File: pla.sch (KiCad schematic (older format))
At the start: 8 parts, among them U12 74LS02, U14 74LS139, U15 74LS175, U16 MOS_251641_PLA

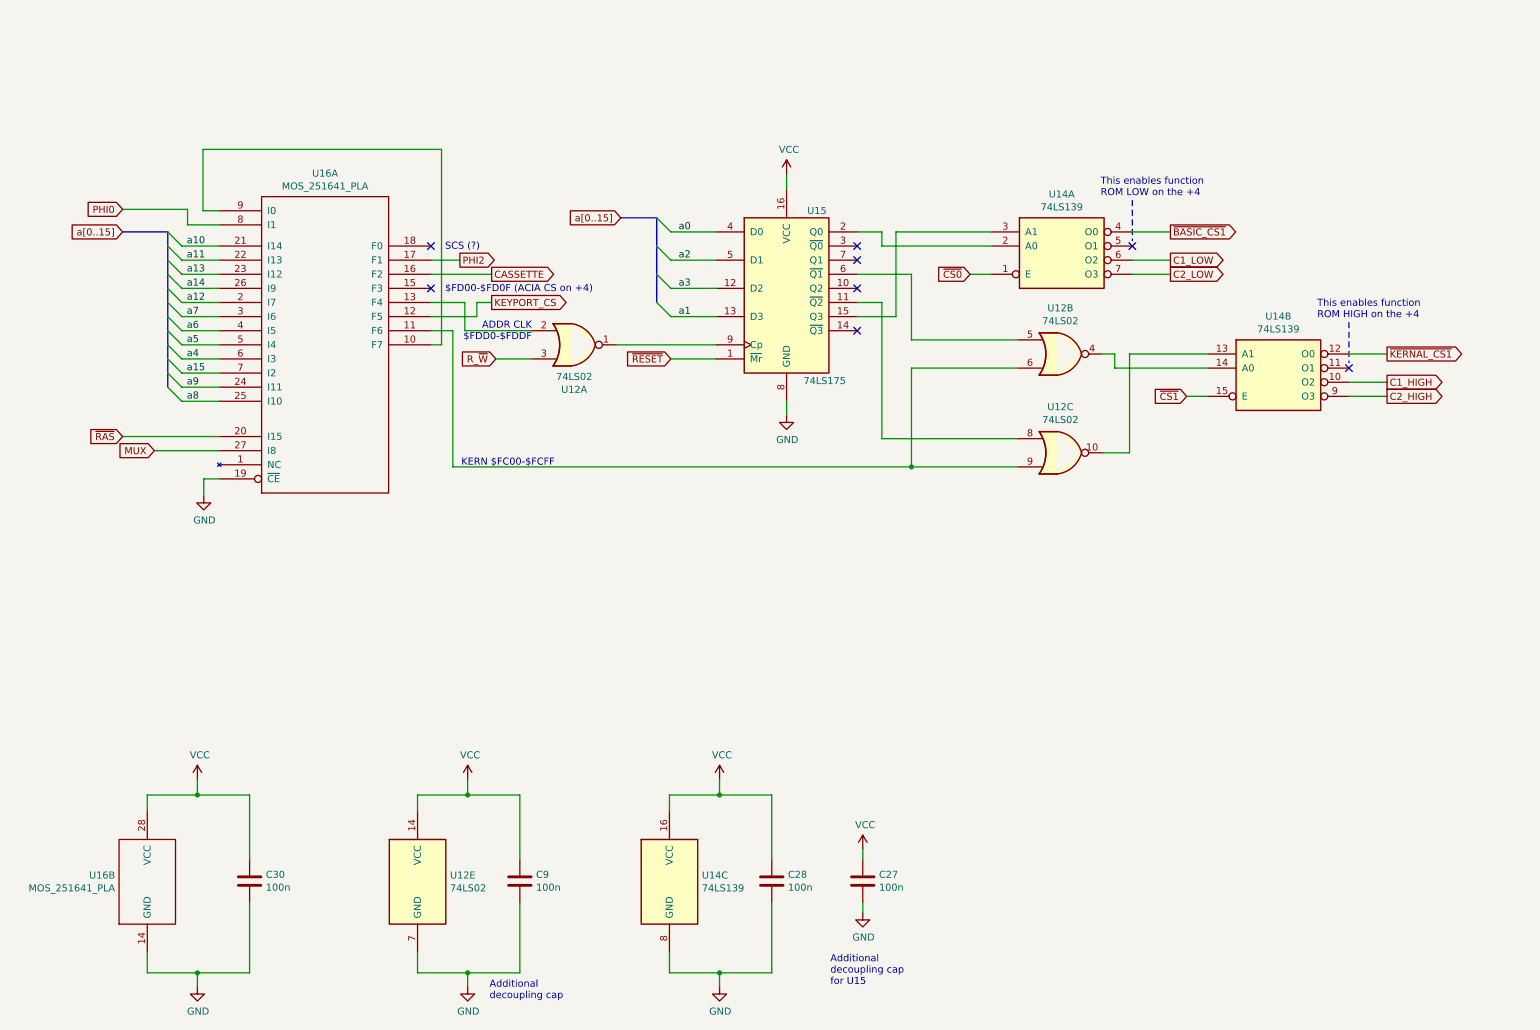
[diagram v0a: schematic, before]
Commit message: Add support for PLA16V8
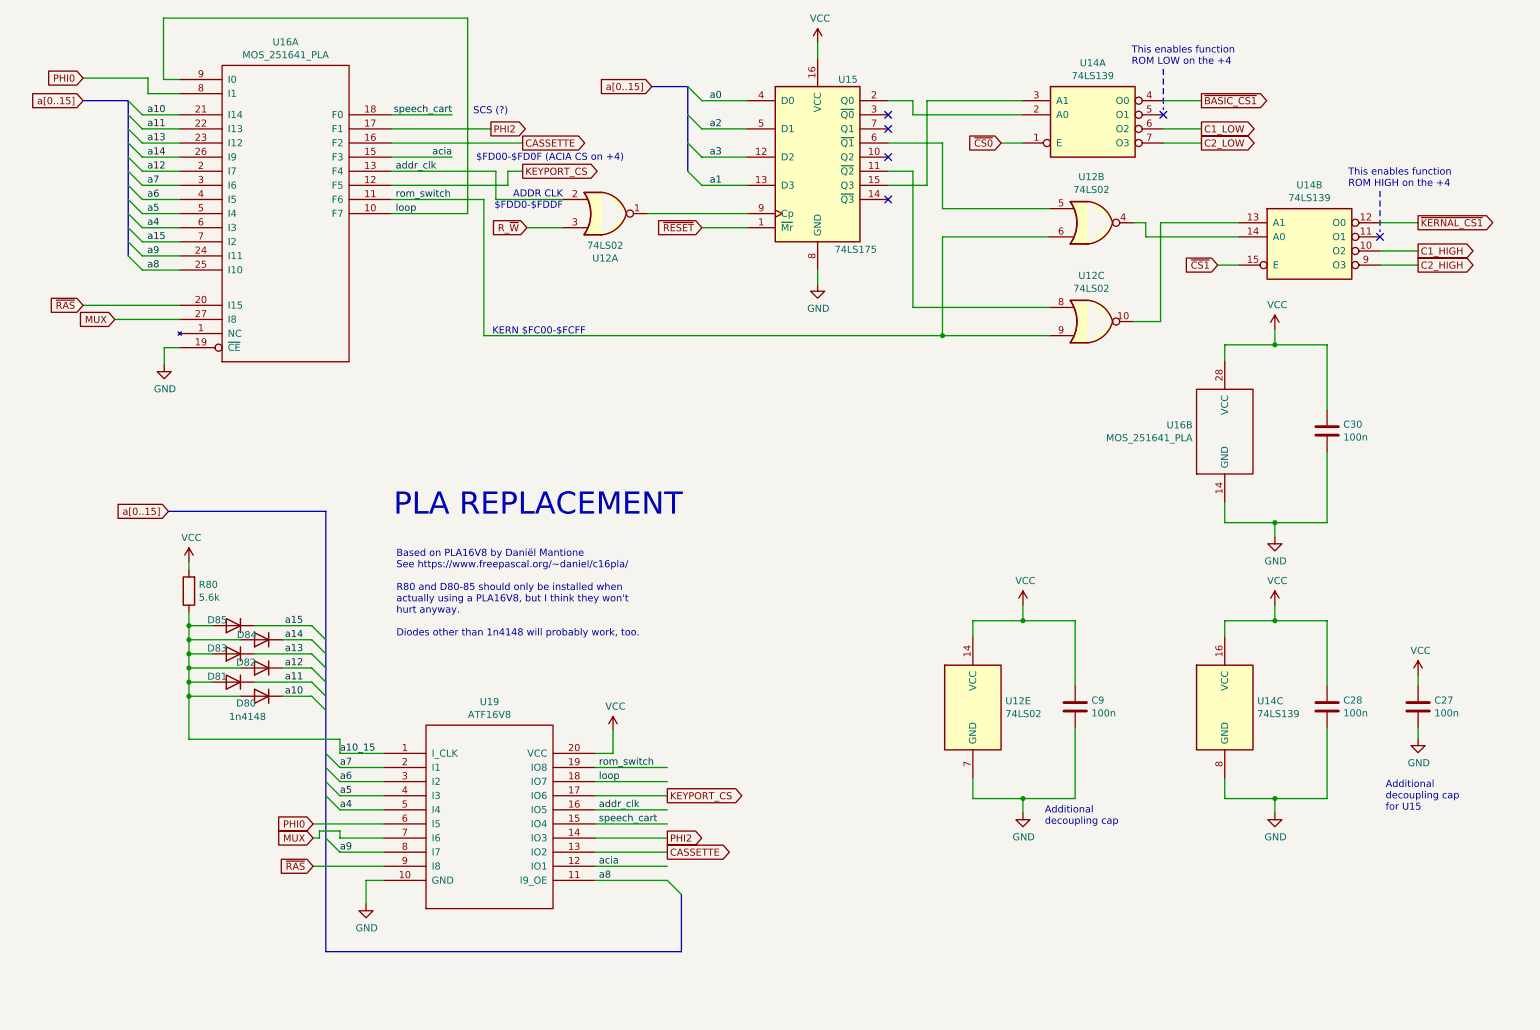
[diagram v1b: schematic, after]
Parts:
- added D80, D81, D82, D83, D84, D85: 1n4148, Diode_THT:D_DO-35_SOD27_P5.08mm_Vertical_KathodeUp, symbol Device:D
- added R80: 5.6k, Resistor_THT:R_Axial_DIN0207_L6.3mm_D2.5mm_P5.08mm_Vertical, symbol Device:R
- added U19: ATF16V8, Package_DIP:DIP-20_W7.62mm_Socket_LongPads, symbol atf16v8:ATF16V8
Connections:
- net labels added: a10_15, acia, addr_clk, loop, rom_switch, speech_cart
- wire segments 105 -> 155
- no-connect marks 8 -> 6
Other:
- note added: "Based on PLA16V8 by Daniël Mantione\nSee https://www.freepascal.org/~~daniel/c16pla/\n\nR80 and D80-85 should only be installed when\nactually using a PLA16V8, but I think they won't\nhurt anyway.\n\nDiodes other than 1n4148 will probably work, too."
- note added: "PLA REPLACEMENT"
- moved on the sheet: C27, C28, C30, C9, U12A, U12B, U12C, U12E, U14A, U14B, U14C, U15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

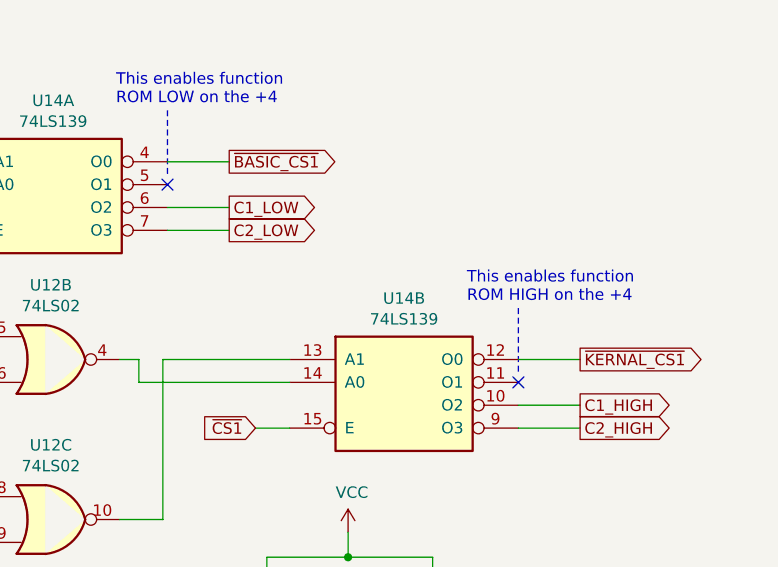
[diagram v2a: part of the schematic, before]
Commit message: Add ability to use a single 64k (EEP)ROM
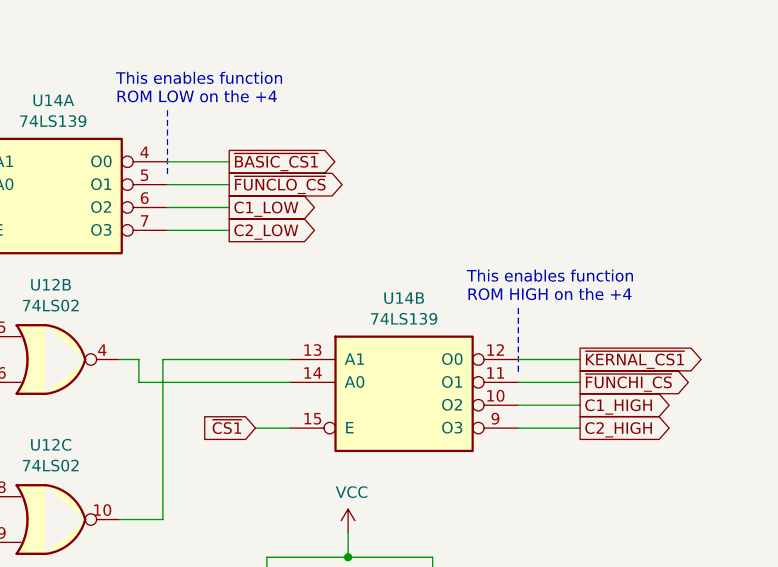
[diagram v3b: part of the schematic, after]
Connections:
- net labels added: ~FUNCHI_CS, ~FUNCLO_CS
- wire segments 155 -> 157
- no-connect marks 6 -> 4
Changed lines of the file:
@@
 	1    0    0    -1
 $EndComp
-NoConn ~ 10150 2150
 Text GLabel 10420 2350 2    50   Output ~ 0
 C2_HIGH
@@
 Wire Wire Line
 	8615 1185 8885 1185
-NoConn ~ 8615 1285
 Wire Wire Line
 	6665 1785 6940 1785
@@
 	1    0    0    -1
 $EndComp
+Text GLabel 8885 1285 2    50   Output ~ 0
+~FUNCLO_CS
+Wire Wire Line
+	8615 1285 8885 1285
+Text GLabel 10420 2150 2    50   Output ~ 0
+~FUNCHI_CS
+Wire Wire Line
+	10150 2150 10420 2150
 Wire Bus Line
 	5245 1085 5245 1685

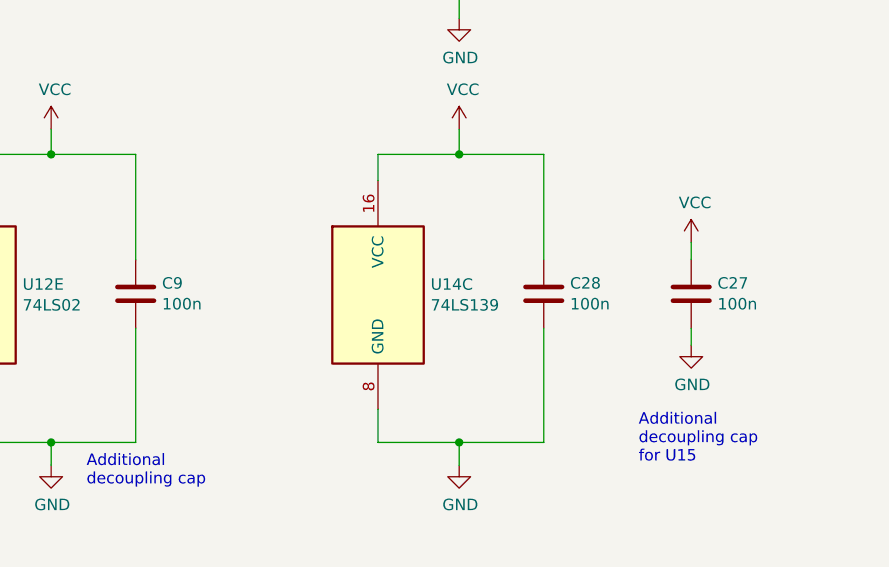
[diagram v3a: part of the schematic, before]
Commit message: Rename extra caps and switch to full THT power circuit Well, there's one SMD component, but it's optional :)
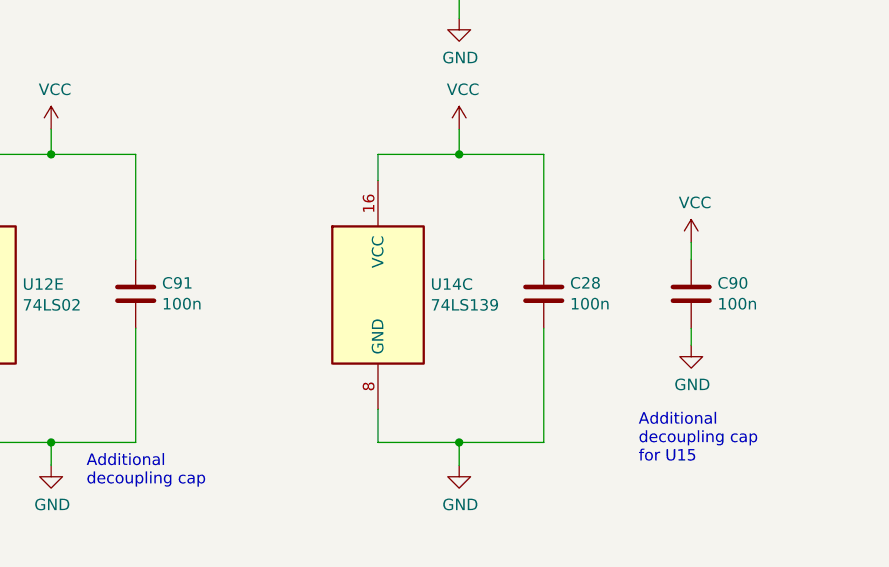
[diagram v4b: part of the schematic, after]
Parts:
- renumbered C27 to C90, C9 to C91
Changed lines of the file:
@@
 	9405 4175 9050 4175
 $Comp
-L Device:C C9
+L Device:C C91
 U 1 1 6116CC87
 P 7990 5480
-F 0 "C9" H 8105 5526 50  0000 L CNN
+F 0 "C91" H 8105 5526 50  0000 L CNN
 F 1 "100n" H 8105 5435 50  0000 L CNN
 F 2 "Capacitor_THT:C_Disc_D8.0mm_W2.5mm_P5.00mm" H 8028 5330 50  0001 C CNN
@@
 P 10420 5480
 AR Path="/5E4A465A/6117E5C3" Ref="C?"  Part="1"
-AR Path="/5EE7AAEB/6117E5C3" Ref="C27"  Part="1"
-F 0 "C27" H 10535 5526 50  0000 L CNN
+AR Path="/5EE7AAEB/6117E5C3" Ref="C90"  Part="1"
+F 0 "C90" H 10535 5526 50  0000 L CNN
 F 1 "100n" H 10535 5435 50  0000 L CNN
 F 2 "Capacitor_THT:C_Disc_D8.0mm_W2.5mm_P5.00mm" H 10458 5330 50  0001 C CNN

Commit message: Add better ESD protection for Datassette Connector and some notes
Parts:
- D80, D81, D82, D83, D84, D85, R80: Notes (none) -> Only mount if using PLA16V8
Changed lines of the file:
@@
 F 2 "Diode_THT:D_DO-35_SOD27_P5.08mm_Vertical_KathodeUp" H 2225 5405 50  0001 C CNN
 F 3 "~" H 2225 5405 50  0001 C CNN
+F 4 "Only mount if using PLA16V8" H 2225 5405 50  0001 C CNN "Notes"
 	1    2225 5405
 	-1   0    0    1
@@
 F 2 "Diode_THT:D_DO-35_SOD27_P5.08mm_Vertical_KathodeUp" H 2025 5305 50  0001 C CNN
 F 3 "~" H 2025 5305 50  0001 C CNN
+F 4 "Only mount if using PLA16V8" H 2025 5305 50  0001 C CNN "Notes"
 	1    2025 5305
 	-1   0    0    1
@@
 F 2 "Diode_THT:D_DO-35_SOD27_P5.08mm_Vertical_KathodeUp" H 2225 5205 50  0001 C CNN
 F 3 "~" H 2225 5205 50  0001 C CNN
+F 4 "Only mount if using PLA16V8" H 2225 5205 50  0001 C CNN "Notes"
 	1    2225 5205
 	-1   0    0    1
@@
 F 2 "Diode_THT:D_DO-35_SOD27_P5.08mm_Vertical_KathodeUp" H 2025 5105 50  0001 C CNN
 F 3 "~" H 2025 5105 50  0001 C CNN
+F 4 "Only mount if using PLA16V8" H 2025 5105 50  0001 C CNN "Notes"
 	1    2025 5105
 	-1   0    0    1
@@
 F 2 "Diode_THT:D_DO-35_SOD27_P5.08mm_Vertical_KathodeUp" H 2225 5005 50  0001 C CNN
 F 3 "~" H 2225 5005 50  0001 C CNN
+F 4 "Only mount if using PLA16V8" H 2225 5005 50  0001 C CNN "Notes"
 	1    2225 5005
 	-1   0    0    1
@@
 F 2 "Diode_THT:D_DO-35_SOD27_P5.08mm_Vertical_KathodeUp" H 2025 4905 50  0001 C CNN
 F 3 "~" H 2025 4905 50  0001 C CNN
+F 4 "Only mount if using PLA16V8" H 2025 4905 50  0001 C CNN "Notes"
 	1    2025 4905
 	-1   0    0    1
@@
 F 2 "Resistor_THT:R_Axial_DIN0207_L6.3mm_D2.5mm_P5.08mm_Vertical" V 1640 4660 50  0001 C CNN
 F 3 "~" H 1710 4660 50  0001 C CNN
+F 4 "Only mount if using PLA16V8" H 1710 4660 50  0001 C CNN "Notes"
 	1    1710 4660
 	-1   0    0    1
